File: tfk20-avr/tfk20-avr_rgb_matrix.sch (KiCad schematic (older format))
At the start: 37 parts, among them U401 IS31FL3733-TQ

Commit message: Add mounting holes
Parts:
- U401: footprint Package_QFP:TQFP-48-1EP_7x7mm_P0.5mm_EP5x5mm -> Package_QFP:TQFP-48-1EP_7x7mm_P0.5mm_EP5x5mm_ThermalVias
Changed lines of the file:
@@
 F 0 "U401" H 10350 1650 50  0000 C CNN
 F 1 "IS31FL3733-TQ" H 10600 1550 50  0000 C CNN
-F 2 "Package_QFP:TQFP-48-1EP_7x7mm_P0.5mm_EP5x5mm" H 9950 3350 50  0001 C CNN
+F 2 "Package_QFP:TQFP-48-1EP_7x7mm_P0.5mm_EP5x5mm_ThermalVias" H 9950 3350 50  0001 C CNN
 F 3 "http://www.issi.com/WW/pdf/IS31FL3733.pdf" H 9950 3350 50  0001 C CNN
 	1    9950 3350
@@
 CS8
 $Comp
-L power:+5V #PWR0120
+L power:+5V #PWR0411
 U 1 1 61383935
 P 9150 1400
-F 0 "#PWR0120" H 9150 1250 50  0001 C CNN
+F 0 "#PWR0411" H 9150 1250 50  0001 C CNN
 F 1 "+5V" H 9165 1573 50  0000 C CNN
 F 2 "" H 9150 1400 50  0001 C CNN
@@
 $EndComp
 $Comp
-L power:+5V #PWR0121
+L power:+5V #PWR0407
 U 1 1 613849FC
 P 7350 1650
-F 0 "#PWR0121" H 7350 1500 50  0001 C CNN
+F 0 "#PWR0407" H 7350 1500 50  0001 C CNN
 F 1 "+5V" H 7365 1823 50  0000 C CNN
 F 2 "" H 7350 1650 50  0001 C CNN

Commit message: Add ISP header
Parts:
- renumbered C407 to C16, C401 to C17, C403 to C18, C405 to C19, C406 to C20, C402 to C21, C404 to C22, D401 to D31, D407 to D32, D413 to D33, D419 to D34, D402 to D35, D408 to D36, D414 to D37, D420 to D38, D403 to D39, D409 to D40, D415 to D41, D421 to D42, D404 to D43, D410 to D44, D416 to D45, D422 to D46, D405 to D47, D411 to D48, D417 to D49, D423 to D50, D406 to D51, D412 to D52, D418 to D53, D424 to D54, R402 to R10, R403 to R11, R404 to R12, R405 to R13, R401 to R9, U401 to U2

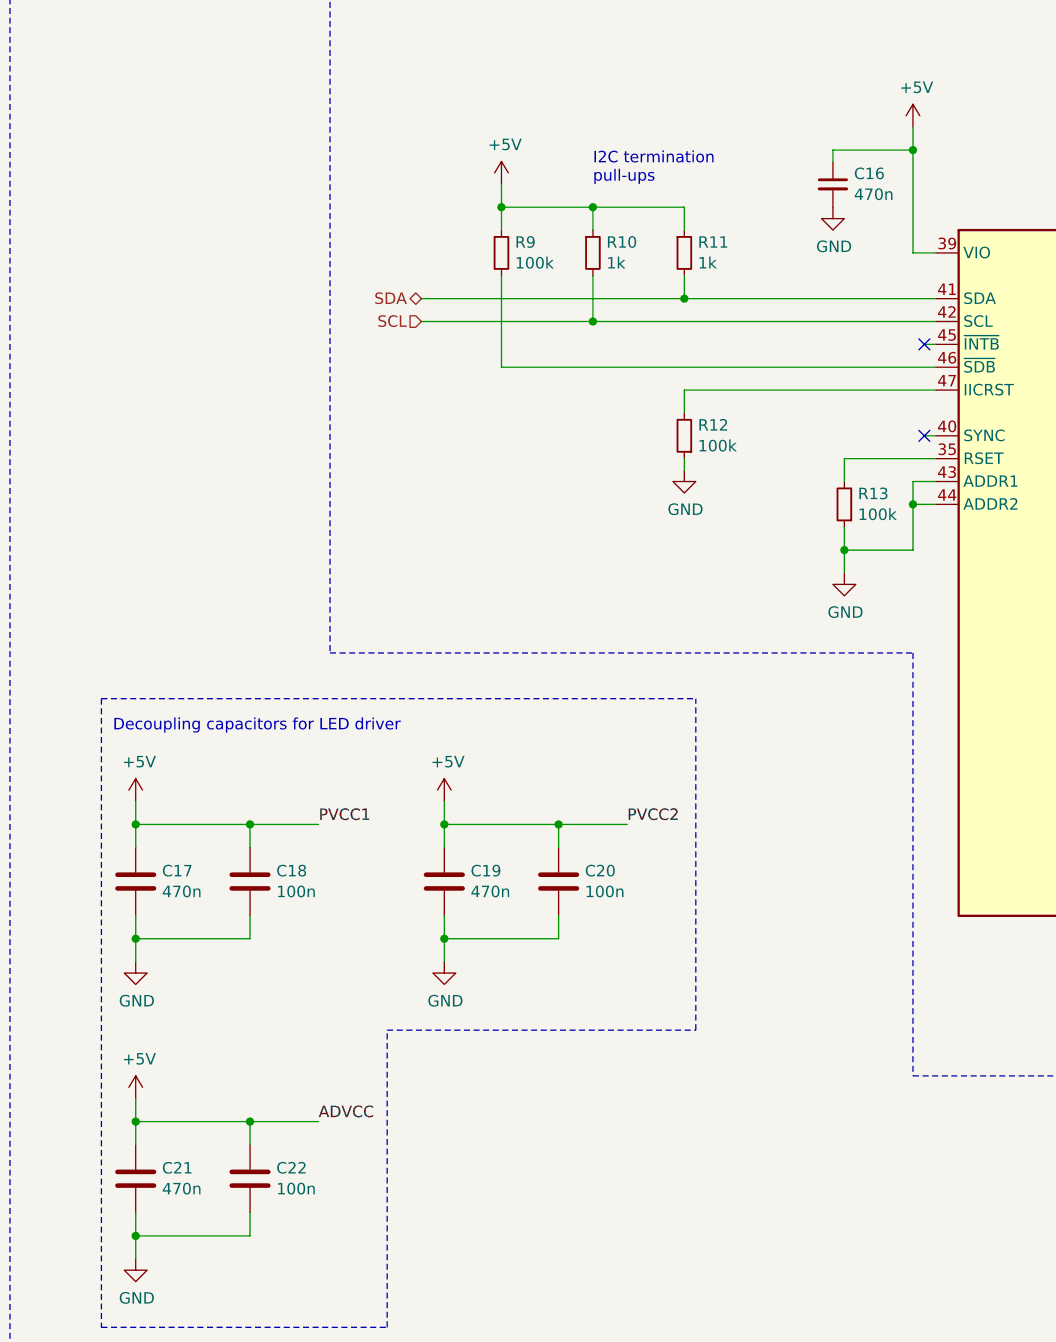
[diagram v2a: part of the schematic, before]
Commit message: Assign some footprints
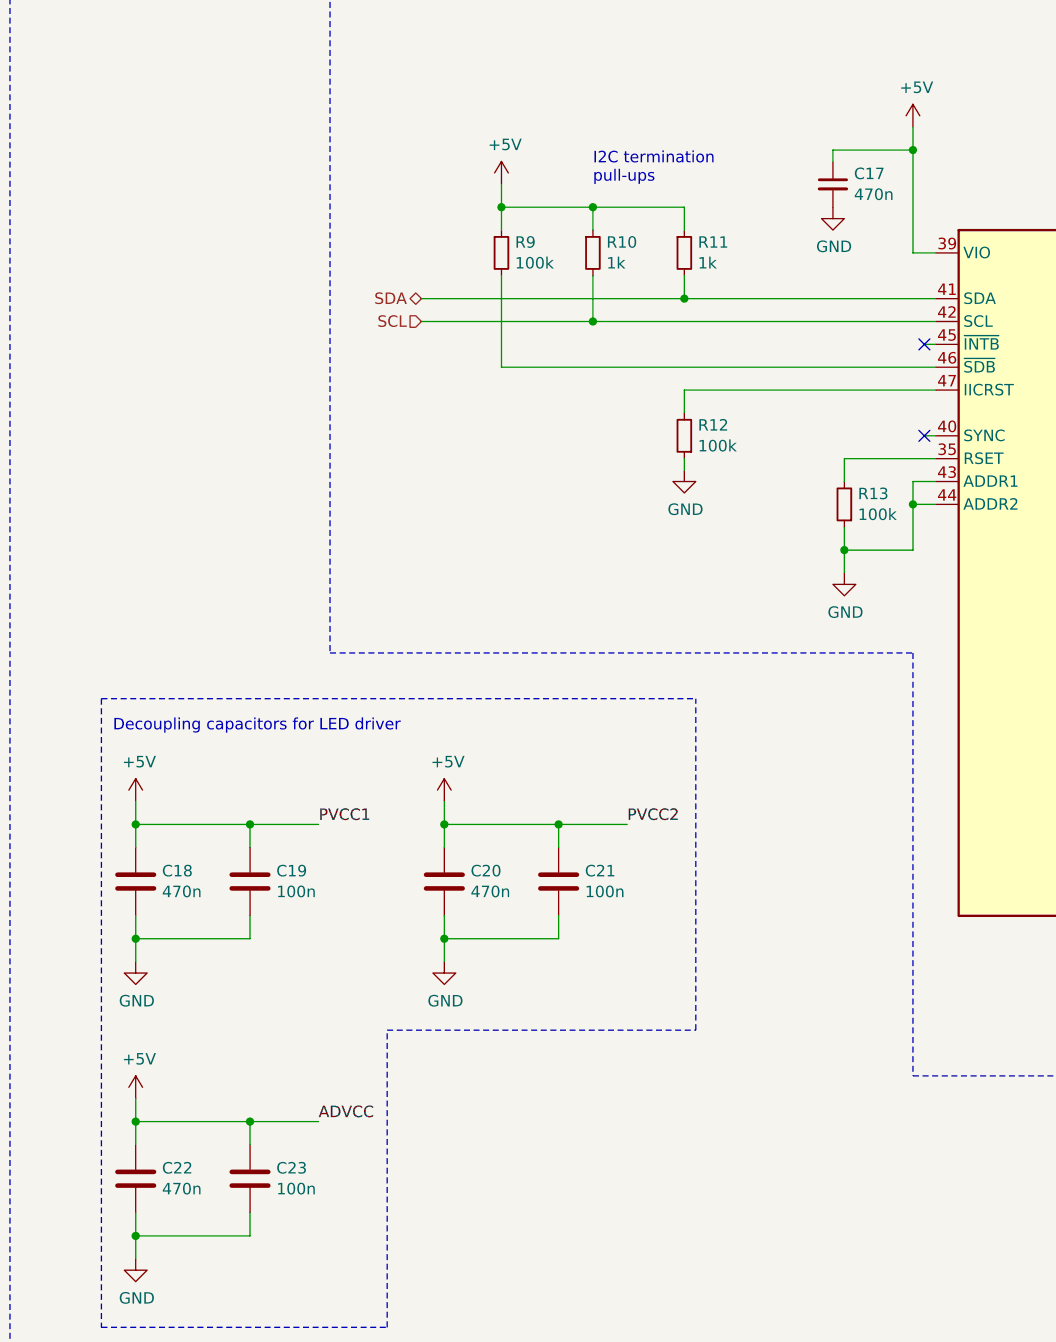
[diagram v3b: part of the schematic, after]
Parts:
- C17: renamed from C16; footprint (none) -> Capacitor_SMD:C_0805_2012Metric_Pad1.18x1.45mm_HandSolder
- C18: renamed from C17; footprint (none) -> Capacitor_SMD:C_0805_2012Metric_Pad1.18x1.45mm_HandSolder
- C19: renamed from C18; footprint (none) -> Capacitor_SMD:C_0805_2012Metric_Pad1.18x1.45mm_HandSolder
- C20: renamed from C19; footprint (none) -> Capacitor_SMD:C_0805_2012Metric_Pad1.18x1.45mm_HandSolder
- C21: renamed from C20; footprint (none) -> Capacitor_SMD:C_0805_2012Metric_Pad1.18x1.45mm_HandSolder
- C22: renamed from C21; footprint (none) -> Capacitor_SMD:C_0805_2012Metric_Pad1.18x1.45mm_HandSolder
- C23: renamed from C22; footprint (none) -> Capacitor_SMD:C_0805_2012Metric_Pad1.18x1.45mm_HandSolder
- R10, R11, R12, R13, R9: footprint (none) -> Resistor_SMD:R_0815_2038Metric_Pad1.20x4.05mm_HandSolder
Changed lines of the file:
@@
 	9150 1950 9250 1950
 $Comp
-L Device:C_Small C16
+L Device:C_Small C17
 U 1 1 602157F1
 P 8800 1650
-F 0 "C16" H 8892 1696 50  0000 L CNN
+F 0 "C17" H 8892 1696 50  0000 L CNN
 F 1 "470n" H 8892 1605 50  0000 L CNN
-F 2 "" H 8800 1650 50  0001 C CNN
+F 2 "Capacitor_SMD:C_0805_2012Metric_Pad1.18x1.45mm_HandSolder" H 8800 1650 50  0001 C CNN
 F 3 "~" H 8800 1650 50  0001 C CNN
 	1    8800 1650
@@
 F 0 "R12" H 8091 2704 50  0000 R CNN
 F 1 "100k" H 8091 2795 50  0000 R CNN
-F 2 "" H 8150 2750 50  0001 C CNN
+F 2 "Resistor_SMD:R_0815_2038Metric_Pad1.20x4.05mm_HandSolder" H 8150 2750 50  0001 C CNN
 F 3 "~" H 8150 2750 50  0001 C CNN
 	1    8150 2750
@@
 F 0 "R9" H 7409 1996 50  0000 L CNN
 F 1 "100k" H 7409 1905 50  0000 L CNN
-F 2 "" H 7350 1950 50  0001 C CNN
+F 2 "Resistor_SMD:R_0815_2038Metric_Pad1.20x4.05mm_HandSolder" H 7350 1950 50  0001 C CNN
 F 3 "~" H 7350 1950 50  0001 C CNN
 	1    7350 1950
@@
 F 0 "R10" H 7809 1996 50  0000 L CNN
 F 1 "1k" H 7809 1905 50  0000 L CNN
-F 2 "" H 7750 1950 50  0001 C CNN
+F 2 "Resistor_SMD:R_0815_2038Metric_Pad1.20x4.05mm_HandSolder" H 7750 1950 50  0001 C CNN
 F 3 "~" H 7750 1950 50  0001 C CNN
 	1    7750 1950
@@
 F 0 "R11" H 8209 1996 50  0000 L CNN
 F 1 "1k" H 8209 1905 50  0000 L CNN
-F 2 "" H 8150 1950 50  0001 C CNN
+F 2 "Resistor_SMD:R_0815_2038Metric_Pad1.20x4.05mm_HandSolder" H 8150 1950 50  0001 C CNN
 F 3 "~" H 8150 1950 50  0001 C CNN
 	1    8150 1950
@@
 F 0 "R13" H 8791 3004 50  0000 R CNN
 F 1 "100k" H 8791 3095 50  0000 R CNN
-F 2 "" H 8850 3050 50  0001 C CNN
+F 2 "Resistor_SMD:R_0815_2038Metric_Pad1.20x4.05mm_HandSolder" H 8850 3050 50  0001 C CNN
 F 3 "~" H 8850 3050 50  0001 C CNN
 	1    8850 3050
@@
 	9950 5050 9950 5150
 $Comp
-L Device:C C17
+L Device:C C18
 U 1 1 60233B22
 P 5750 4700
-F 0 "C17" H 5865 4746 50  0000 L CNN
+F 0 "C18" H 5865 4746 50  0000 L CNN
 F 1 "470n" H 5865 4655 50  0000 L CNN
-F 2 "" H 5788 4550 50  0001 C CNN
+F 2 "Capacitor_SMD:C_0805_2012Metric_Pad1.18x1.45mm_HandSolder" H 5788 4550 50  0001 C CNN
 F 3 "~" H 5750 4700 50  0001 C CNN
 	1    5750 4700
@@
 $EndComp
 $Comp
-L Device:C C18
+L Device:C C19
 U 1 1 60234E7C
 P 6250 4700
-F 0 "C18" H 6365 4746 50  0000 L CNN
+F 0 "C19" H 6365 4746 50  0000 L CNN
 F 1 "100n" H 6365 4655 50  0000 L CNN
-F 2 "" H 6288 4550 50  0001 C CNN
+F 2 "Capacitor_SMD:C_0805_2012Metric_Pad1.18x1.45mm_HandSolder" H 6288 4550 50  0001 C CNN
 F 3 "~" H 6250 4700 50  0001 C CNN
 	1    6250 4700
@@
 PVCC1
 $Comp
-L Device:C C19
+L Device:C C20
 U 1 1 6023CACA
 P 7100 4700
-F 0 "C19" H 7215 4746 50  0000 L CNN
+F 0 "C20" H 7215 4746 50  0000 L CNN
 F 1 "470n" H 7215 4655 50  0000 L CNN
-F 2 "" H 7138 4550 50  0001 C CNN
+F 2 "Capacitor_SMD:C_0805_2012Metric_Pad1.18x1.45mm_HandSolder" H 7138 4550 50  0001 C CNN
 F 3 "~" H 7100 4700 50  0001 C CNN
 	1    7100 4700
@@
 $EndComp
 $Comp
-L Device:C C20
+L Device:C C21
 U 1 1 6023CAD0
 P 7600 4700
-F 0 "C20" H 7715 4746 50  0000 L CNN
+F 0 "C21" H 7715 4746 50  0000 L CNN
 F 1 "100n" H 7715 4655 50  0000 L CNN
-F 2 "" H 7638 4550 50  0001 C CNN
+F 2 "Capacitor_SMD:C_0805_2012Metric_Pad1.18x1.45mm_HandSolder" H 7638 4550 50  0001 C CNN
 F 3 "~" H 7600 4700 50  0001 C CNN
 	1    7600 4700
@@
 PVCC2
 $Comp
-L Device:C C21
+L Device:C C22
 U 1 1 6023EA0C
 P 5750 6000
-F 0 "C21" H 5865 6046 50  0000 L CNN
+F 0 "C22" H 5865 6046 50  0000 L CNN
 F 1 "470n" H 5865 5955 50  0000 L CNN
-F 2 "" H 5788 5850 50  0001 C CNN
+F 2 "Capacitor_SMD:C_0805_2012Metric_Pad1.18x1.45mm_HandSolder" H 5788 5850 50  0001 C CNN
 F 3 "~" H 5750 6000 50  0001 C CNN
 	1    5750 6000
@@
 $EndComp
 $Comp
-L Device:C C22
+L Device:C C23
 U 1 1 6023EA12
 P 6250 6000
-F 0 "C22" H 6135 5954 50  0000 R CNN
+F 0 "C23" H 6135 5954 50  0000 R CNN
 F 1 "100n" H 6135 6045 50  0000 R CNN
-F 2 "" H 6288 5850 50  0001 C CNN
+F 2 "Capacitor_SMD:C_0805_2012Metric_Pad1.18x1.45mm_HandSolder" H 6288 5850 50  0001 C CNN
 F 3 "~" H 6250 6000 50  0001 C CNN
 	1    6250 6000

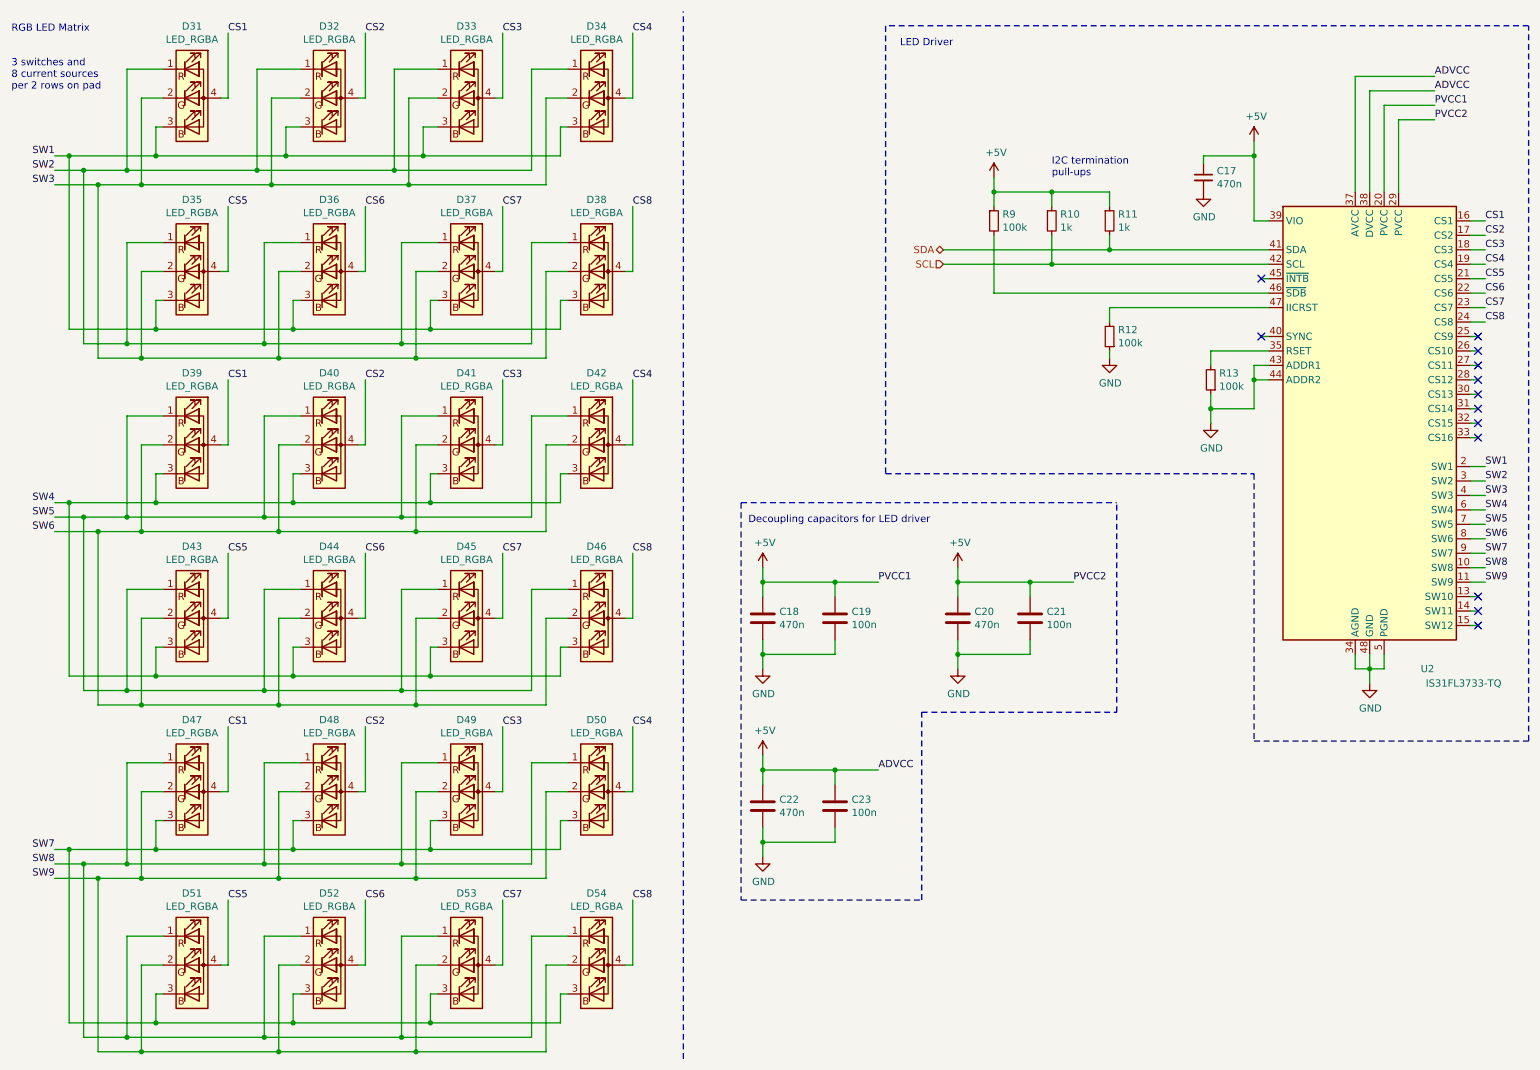
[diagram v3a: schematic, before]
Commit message: Remove alternative LEDs
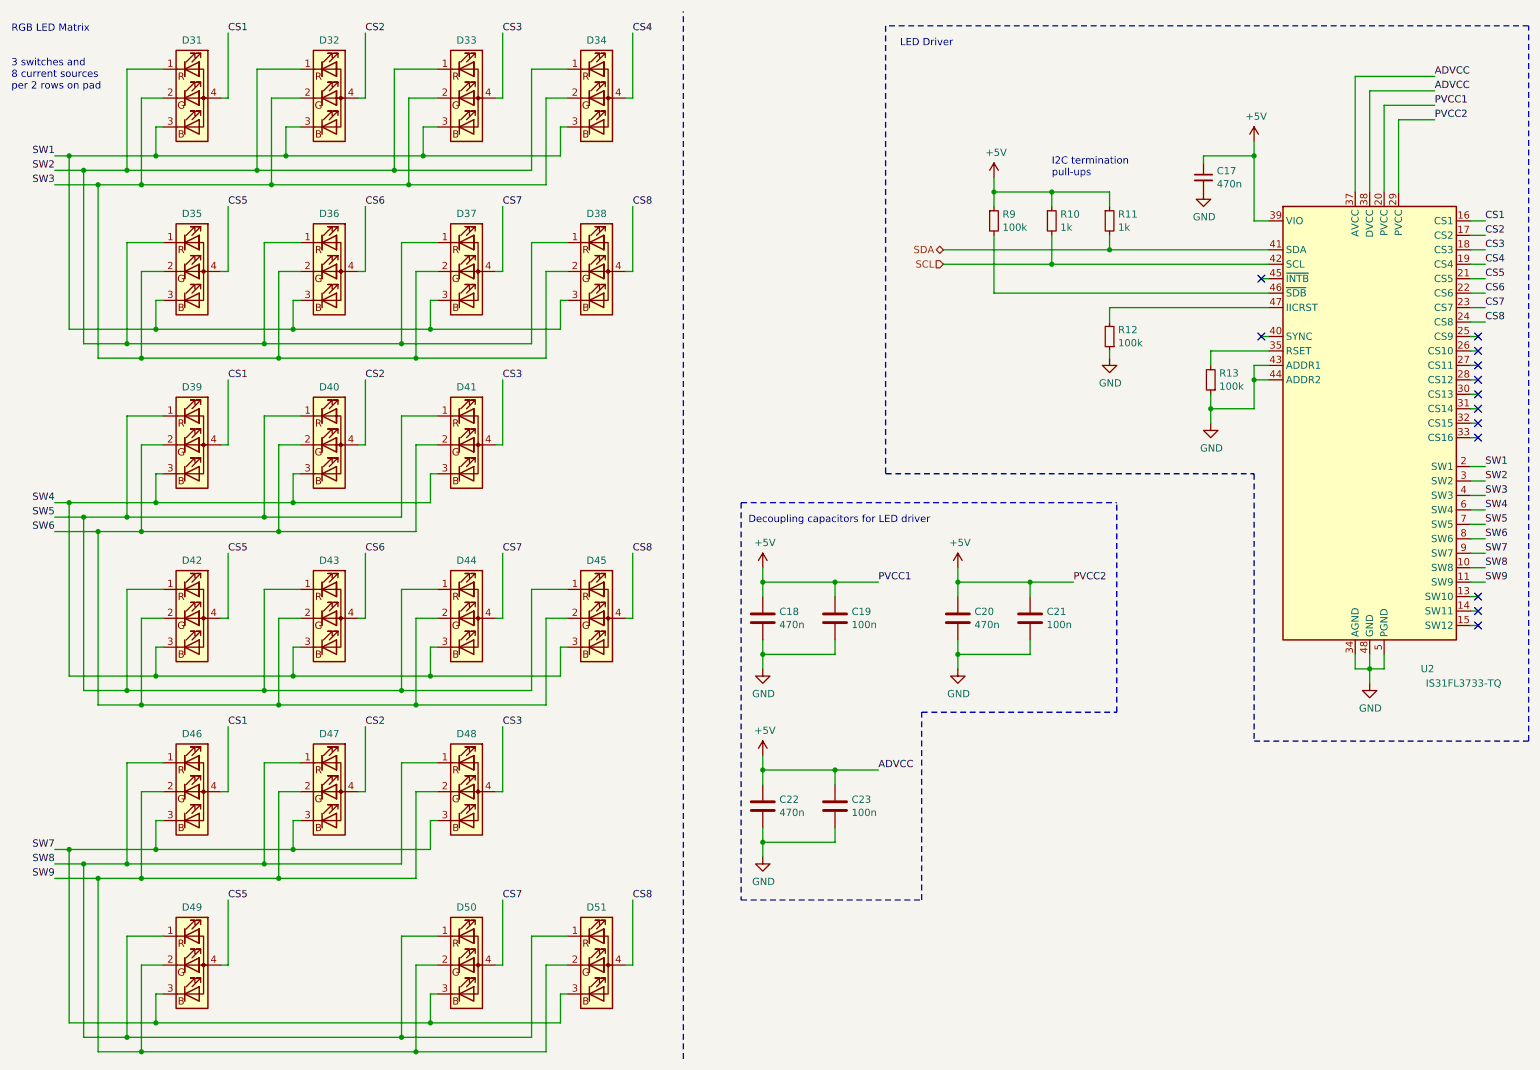
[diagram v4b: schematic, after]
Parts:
- removed D42, D50, D52: LED_RGBA, symbol Device:LED_RGBA
- renumbered D43 to D42, D44 to D43, D45 to D44, D46 to D45, D47 to D46, D48 to D47, D49 to D48, D51 to D49, D53 to D50, D54 to D51
